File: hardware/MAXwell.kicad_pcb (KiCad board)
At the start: 2 copper layers, 85.9 x 96.1 mm, 155 parts, among them J1 Conn_02x05_Odd_Even, J2 Conn_02x12_Counter_Clockwise, J3 Barrel_Jack_Switch_Pin3Ring, SW1 SW_Push_Dual, SW10 SW_Wuerth_450301014042, SW11 SW_Wuerth_450301014042, SW12 SW_Wuerth_450301014042, SW13 SW_Wuerth_450301014042, SW2 SW_Push_Dual, SW3 SW_Push_Dual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

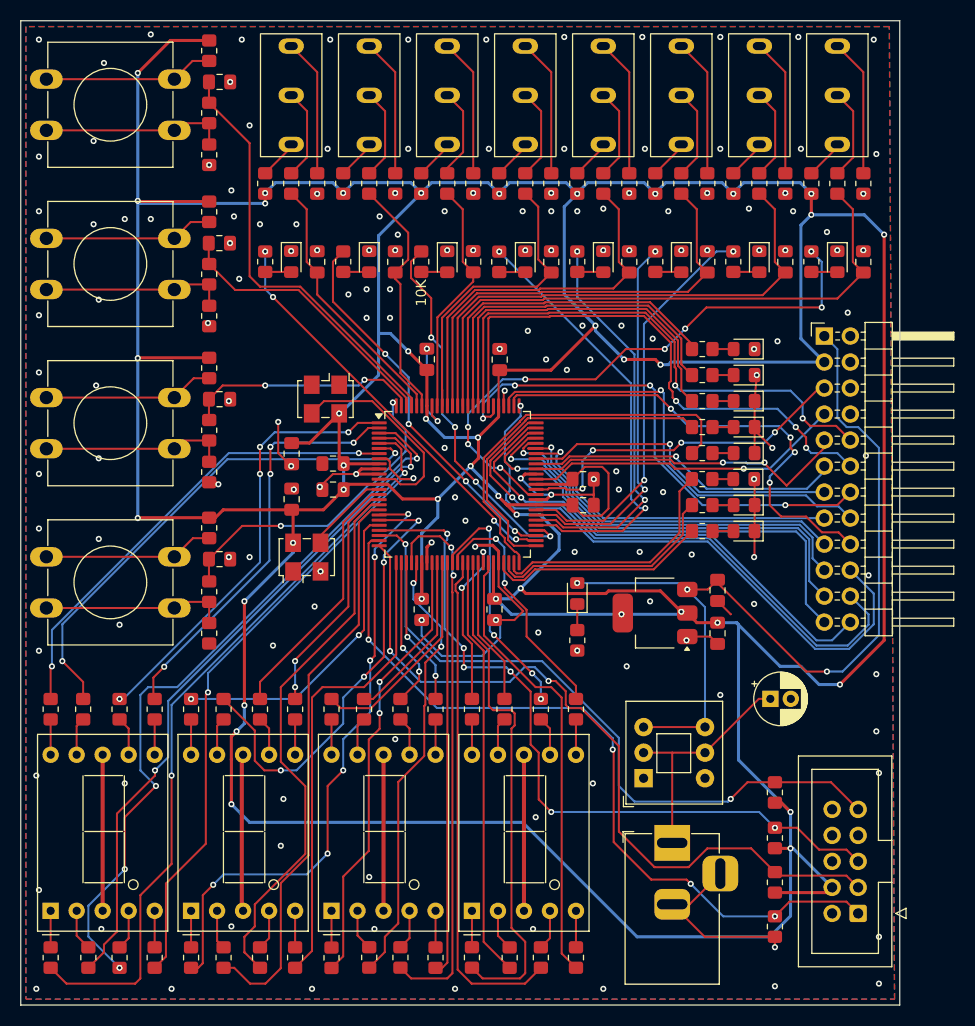
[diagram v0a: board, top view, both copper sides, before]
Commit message: put values on silk screen
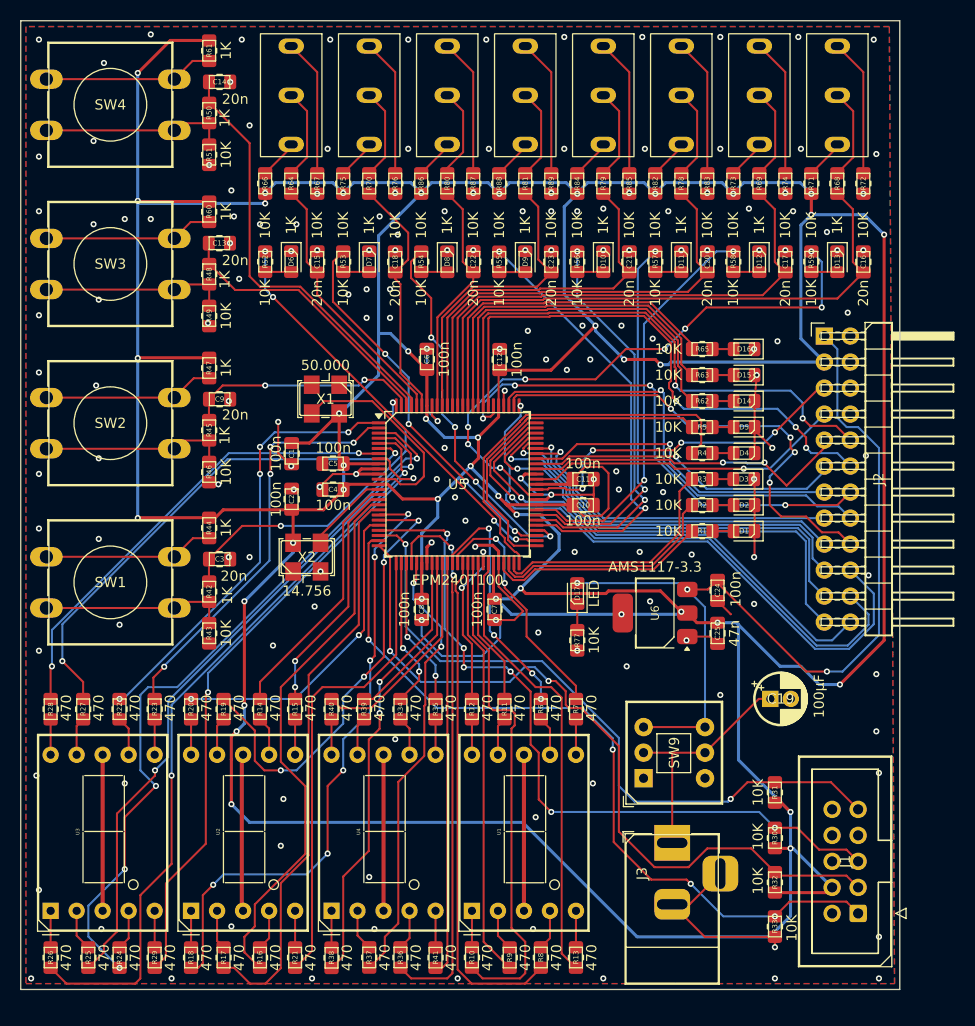
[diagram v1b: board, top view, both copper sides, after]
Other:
- board size 85.9 x 96.1 mm -> 85.9 x 94.6 mm
